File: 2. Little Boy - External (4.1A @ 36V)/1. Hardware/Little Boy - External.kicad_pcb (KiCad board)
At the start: 4 copper layers, 67.2 x 46.8 mm, 65 parts, among them IC1 DRV8251DDAR, IC2 AS5600-ASOT, J10 Conn_01x06_MountingPin, J11 Conn_01x06_MountingPin, J3 Power_In, J4 Power_In, J5 MOT_B, J6 MOT_A, J7 Conn_01x06_MountingPin, J8 Control_In, J9 Control_In, U1 STM32G0B1CBTx, U2 LMR33630CDDA, U3 TLV76733DRVx, U4 TJA1051T-3, U5 MA730, Y1 Crystal_GND24

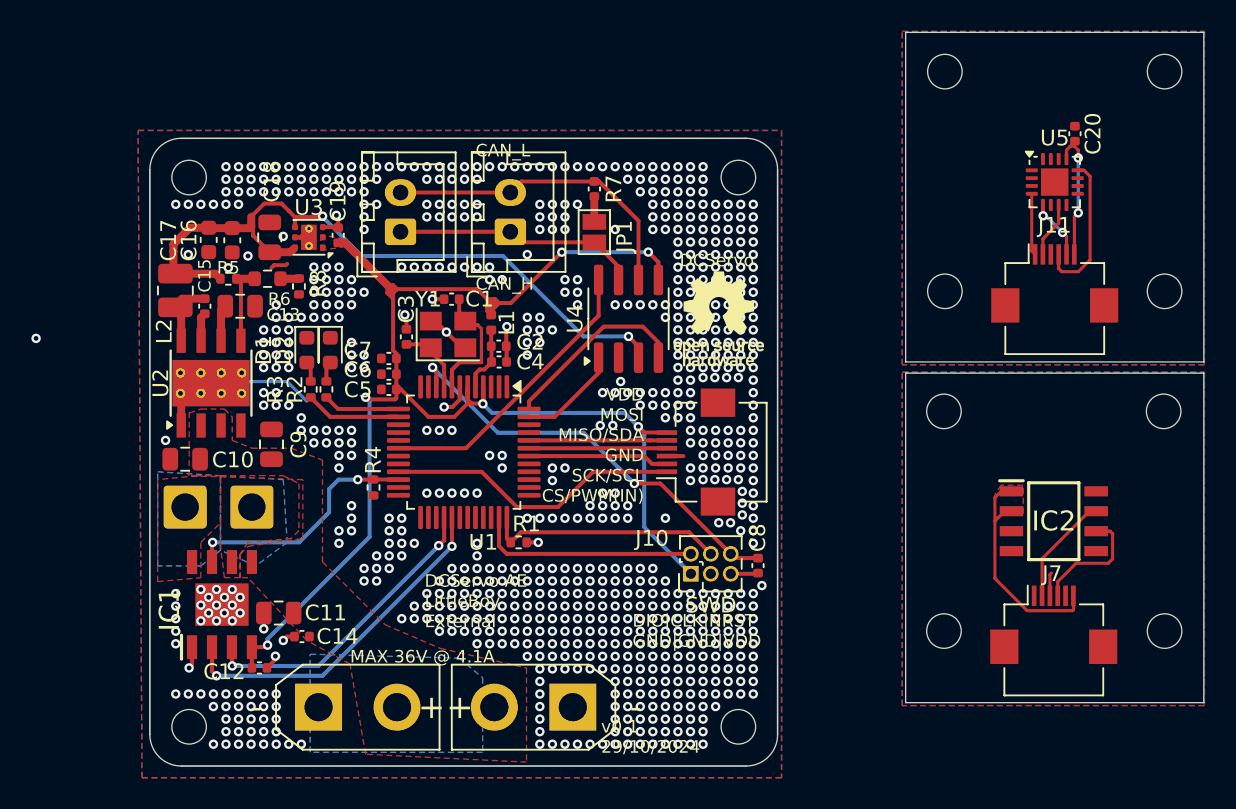
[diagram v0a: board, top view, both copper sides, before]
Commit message: Esthetic Changes, Fix-up of daughter boards.
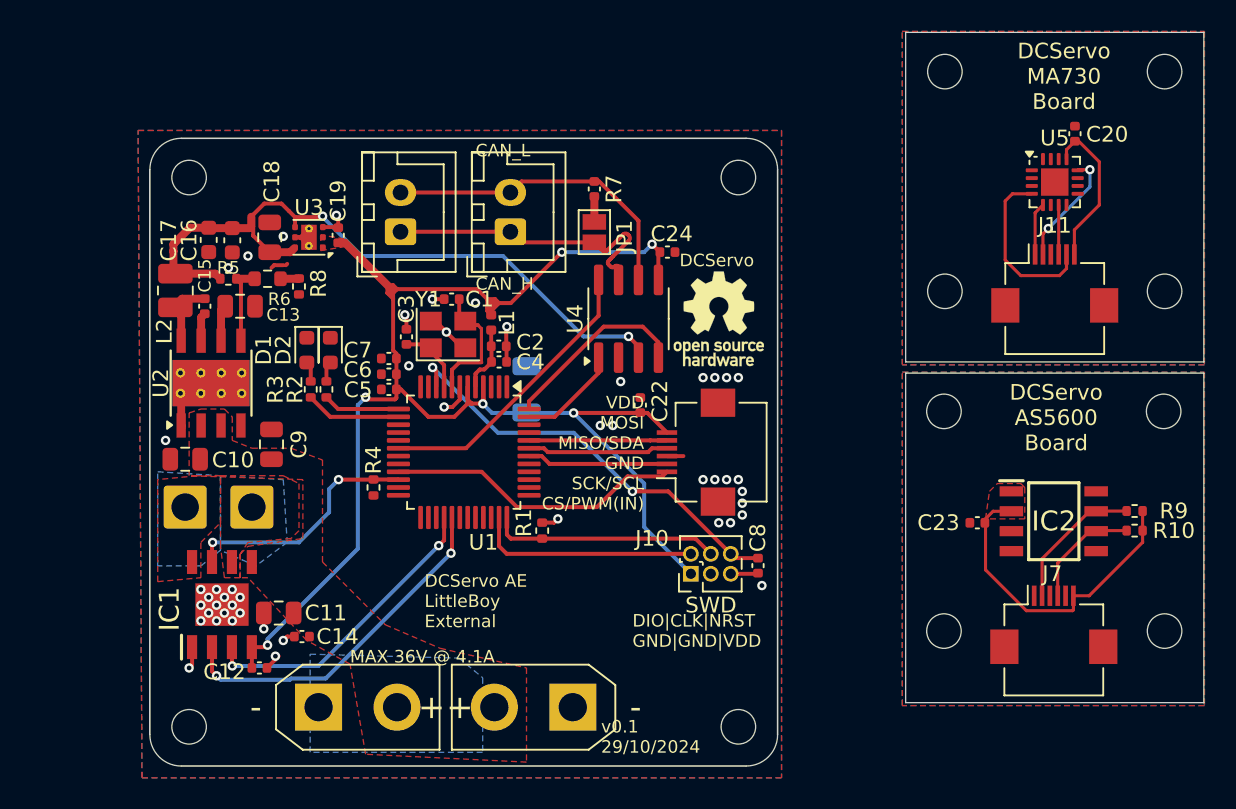
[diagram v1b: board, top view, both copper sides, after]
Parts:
- added C21: 100nF, Capacitor_SMD:C_1206_3216Metric, B.Cu at (147.0, 59.0)
- added C22: 100nF, Capacitor_SMD:C_0402_1005Metric, F.Cu at (154.2, 60.0)
- added C23: 100nF, Capacitor_SMD:C_0402_1005Metric, F.Cu at (175.7, 67.5)
- added C24: 100nF, Capacitor_SMD:C_0402_1005Metric, F.Cu at (156.0, 50.2)
- added R10: 4.7k, Resistor_SMD:R_0402_1005Metric, F.Cu at (185.8, 68.0)
- added R9: 4.7k, Resistor_SMD:R_0402_1005Metric, F.Cu at (185.8, 66.8)
- added REF**: , Symbol:OSHW-Logo_19x20mm_SilkScreen, B.Cu at (180.8, 68.5)
- added REF**: OSHW-Logo_19x20mm_SilkScreen, Symbol:OSHW-Logo_19x20mm_SilkScreen, B.Cu at (180.8, 46.8)
- moved R1 1.68 mm to (148.0, 68.0), turned to 90 degrees
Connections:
- U5 pad 12: Net-(J11-Pin_4) -> Net-(J11-Pin_2)
- U5 pad 4: Net-(J11-Pin_1) -> Net-(J11-Pin_5)
- U5 pad 5: Net-(J11-Pin_5) -> Net-(J11-Pin_1)
- U5 pad 7: Net-(J11-Pin_2) -> Net-(J11-Pin_4)
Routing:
- net Net-(J11-Pin_5): track 4.29 -> 11.0 mm, vias 2 -> 0
- net GND: track 31.3 -> 24.9 mm, vias 770 -> 49
- net Net-(J11-Pin_4): track 9.57 -> 3.15 mm
- net +3.3VP: track 14.4 -> 20.5 mm
- net CAN_H: track 15.7 -> 19.6 mm
- net Net-(J11-Pin_2): track 3.56 -> 7.43 mm, vias 0 -> 2
- net +3V3: track 95.1 -> 98.3 mm
- net Encoder_SCL: track 7.06 -> 9.01 mm
- net +3.3V: track 8.29 -> 10.0 mm, vias 2 -> 0
- net GND2: track 1.49 -> 0.00 mm
- net (no net): track 0.94 -> 0.00 mm, vias 1 -> 0
- net SWCLK: track 15.3 -> 14.6 mm
- net Net-(J11-Pin_1): track 3.95 -> 3.36 mm
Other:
- board text added: "DCServo AS5600 Board"
- board text added: "DCServo MA730 Board"

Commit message: V2.2 - Added Test Points, fixed DFM Errors
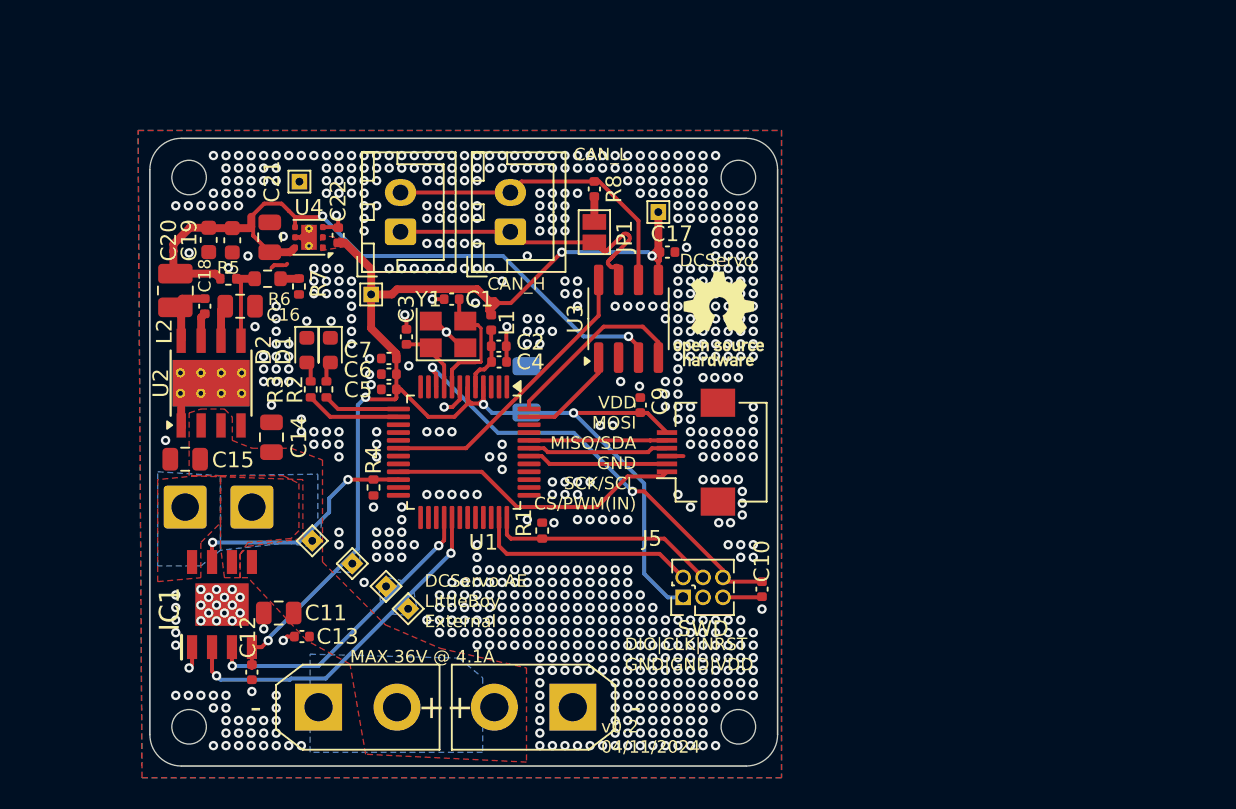
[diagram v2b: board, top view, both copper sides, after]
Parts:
- removed the C20 at (181.9, 42.7)
- removed C23: 100nF, Capacitor_SMD:C_0402_1005Metric
- removed H11, H5, H8, H9: MountingHole, MountingHole:MountingHole_2.2mm_M2
- removed the H12 at (187.7, 74.4)
- removed the H2 at (187.7, 52.8)
- removed the H3 at (173.6, 60.4)
- removed the H6 at (187.6, 60.4)
- removed IC2: AS5600-ASOT, KiCadLibrary:SOIC127P600X175-8N
- removed the J11 at (180.7, 52.2)
- removed R10, R9: 4.7k, Resistor_SMD:R_0402_1005Metric
- removed the REF** at (180.8, 68.5)
- removed the REF** at (180.8, 46.8)
- removed U5: MA730, Package_DFN_QFN:QFN-16-1EP_3x3mm_P0.5mm_EP1.75x1.75mm
- added J1: Conn_01x01, TestPoint:TestPoint_THTPad_1.0x1.0mm_Drill0.5mm, F.Cu at (137.1, 53.0)
- added J12: Conn_01x01, TestPoint:TestPoint_THTPad_1.0x1.0mm_Drill0.5mm, F.Cu at (132.5, 45.8)
- added J17: Conn_01x01, TestPoint:TestPoint_THTPad_1.0x1.0mm_Drill0.5mm, F.Cu at (133.3, 68.7)
- added J2: Conn_01x01, TestPoint:TestPoint_THTPad_1.0x1.0mm_Drill0.5mm, F.Cu at (155.4, 47.7)
- added J3: Conn_01x01, TestPoint:TestPoint_THTPad_1.0x1.0mm_Drill0.5mm, F.Cu at (135.9, 70.1)
- added J6: Conn_01x01, TestPoint:TestPoint_THTPad_1.0x1.0mm_Drill0.5mm, F.Cu at (139.5, 73.0)
- J7: value Conn_01x06_MountingPin -> Conn_01x01; footprint Connector_FFC-FPC:Hirose_FH12-6S-0.5SH_1x06-1MP_P0.50mm_Horizontal -> TestPoint:TestPoint_THTPad_1.0x1.0mm_Drill0.5mm
- moved J7 42.6 mm to (138.1, 71.5), turned to 45 degrees
- moved SWD 1.58 mm to (157.0, 72.2)
- moved C10 1.52 mm to (162.0, 71.7)
- moved C12 0.55 mm to (129.5, 77.0), turned to 90 degrees
- moved C14 0.45 mm to (130.8, 62.0)
- renumbered C8 to C10, C14 to C13, C9 to C14, C10 to C15, C13 to C16, C24 to C17, C15 to C18, C16 to C19, C17 to C20, C18 to C21, C19 to C22, C21 to C8, C22 to C9, D2 to D1, D1 to D2, H4 to H12, H1 to H2, H7 to H3, H10 to H6, J5 to J10, J6 to J11, J8 to J13, J9 to J14, J10 to J5, J3 to J8, J4 to J9, R8 to R7, R7 to R8, U4 to U3, U3 to U4
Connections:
- J7 pad 1: unconnected-(J7-Pin_1-Pad1) -> DRV_IN1
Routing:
- net +3.3VP: track 20.5 -> 0.00 mm
- net Net-(J11-Pin_5): track 11.0 -> 0.00 mm
- net +3.3V: track 10.0 -> 0.00 mm
- net Encoder_SCL: track 9.01 -> 0.00 mm
- net Net-(J11-Pin_2): track 7.43 -> 0.00 mm, vias 2 -> 0
- net Encoder_SDA: track 7.33 -> 0.00 mm
- net +3V3: track 98.3 -> 102.0 mm
- net Net-(J11-Pin_1): track 3.36 -> 0.00 mm
- net Net-(J11-Pin_4): track 3.15 -> 0.00 mm
- net GND: track 24.9 -> 22.5 mm, vias 49 -> 716
- net NRST: track 27.1 -> 28.0 mm
- added copper zone on B.Cu, net +3V3
- added copper zone on B.Cu, net DRV_IN1
- added copper zone on B.Cu, net DRV_IN2
- added copper zone on B.Cu, net ISEN
- removed copper zone on F.Cu, net +3.3VP
- removed copper zone on B.Cu, net GND1
- removed copper zone on F.Cu, net GND1
- removed copper zone on In1.Cu, net GND1
- removed copper zone on In2.Cu, net GND1
- removed copper zone on B.Cu, net GND2
- removed copper zone on F.Cu, net GND2
- removed copper zone on In1.Cu, net GND2
- removed copper zone on In2.Cu, net GND2
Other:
- board size 67.2 x 46.8 mm -> 40 x 40 mm
- board text added: "v0.2 04/11/2024"
- board text removed: "DCServo AS5600 Board"
- board text removed: "DCServo MA730 Board"
- board text removed: "v0.1 29/10/2024"

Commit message: up
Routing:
- net Net-(IC1-OUT2): vias 0 -> 2
- net GND: vias 716 -> 728
- net  MOT_A: vias 0 -> 3
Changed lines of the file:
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@@
 	)
 	(via
+		(at 124 74)
+		(size 0.6)
+		(drill 0.3)
+		(layers "F.Cu" "B.Cu")
+		(free yes)
+		(net 2)
+	)
+	(via
 		(at 147.85 56.1)
 		(size 0.6)
@@
 	)
 	(via
+		(at 125 78)
+		(size 0.6)
+		(drill 0.3)
+		(layers "F.Cu" "B.Cu")
+		(free yes)
+		(net 2)
+	)
+	(via
 		(at 159.05 63.3)
 		(size 0.6)
@@
 	)
 	(via
+		(at 130.5 76)
+		(size 0.6)
+		(drill 0.3)
+		(layers "F.Cu" "B.Cu")
+		(free yes)
+		(net 2)
+	)
+	(via
 		(at 134.887498 47.909178)
 		(size 0.6)
@@
 	)
 	(via
+		(at 124.5 76.5)
+		(size 0.6)
+		(drill 0.3)
+		(layers "F.Cu" "B.Cu")
+		(free yes)
+		(net 2)
+	)
+	(via
 		(at 147.85 73.7)
 		(size 0.6)
@@
 	)
 	(via
+		(at 132.5 76)
+		(size 0.6)
+		(drill 0.3)
+		(layers "F.Cu" "B.Cu")
+		(free yes)
+		(net 2)
+	)
+	(via
 		(at 150.25 52.9)
 		(size 0.6)
@@
 	)
 	(via
+		(at 124 75)
+		(size 0.6)
+		(drill 0.3)
+		(layers "F.Cu" "B.Cu")
+		(free yes)
+		(net 2)
+	)
+	(via
 		(at 153 58.5)
 		(size 0.6)
@@
 	)
 	(via
+		(at 125.5 77.5)
+		(size 0.6)
+		(drill 0.3)
+		(layers "F.Cu" "B.Cu")
+		(free yes)
+		(net 2)
+	)
+	(via
 		(at 148.65 72.1)
 		(size 0.6)
@@
 	)
 	(via
+		(at 131.5 76)
+		(size 0.6)
+		(drill 0.3)
+		(layers "F.Cu" "B.Cu")
+		(free yes)
+		(net 2)
+	)
+	(via
 		(at 157.45 77.7)
 		(size 0.6)
@@
 	)
 	(via
+		(at 124 77)
+		(size 0.6)
+		(drill 0.3)
+		(layers "F.Cu" "B.Cu")
+		(free yes)
+		(net 2)
+	)
+	(via
 		(at 139.05 69.7)
 		(size 0.6)
@@
 	)
 	(via
+		(at 124 72.5)
+		(size 0.6)
+		(drill 0.3)
+		(layers "F.Cu" "B.Cu")
+		(free yes)
+		(net 2)
+	)
+	(via
 		(at 159.05 76.9)
 		(size 0.6)
@@
 	)
 	(via
+		(at 124 76)
+		(size 0.6)
+		(drill 0.3)
+		(layers "F.Cu" "B.Cu")
+		(free yes)
+		(net 2)
+	)
+	(via
 		(at 147.85 81.7)
 		(size 0.6)
@@
 	)
 	(via
+		(at 124.5 77.5)
+		(size 0.6)
+		(drill 0.3)
+		(layers "F.Cu" "B.Cu")
+		(free yes)
+		(net 2)
+	)
+	(via
 		(at 148.65 46.5)
 		(size 0.6)
@@
 		(net 13)
 	)
+	(via
+		(at 124 69)
+		(size 0.6)
+		(drill 0.3)
+		(layers "F.Cu" "B.Cu")
+		(free yes)
+		(net 14)
+	)
+	(via
+		(at 124 70)
+		(size 0.6)
+		(drill 0.3)
+		(layers "F.Cu" "B.Cu")
+		(free yes)
+		(net 14)
+	)
 	(segment
 		(start 142.1875 69.4375)
@@
 		(net 59)
 	)
+	(via
+		(at 132 67.5)
+		(size 0.6)
+		(drill 0.3)
+		(layers "F.Cu" "B.Cu")
+		(free yes)
+		(net 62)
+	)
+	(via
+		(at 132 66.5)
+		(size 0.6)
+		(drill 0.3)
+		(layers "F.Cu" "B.Cu")
+		(free yes)
+		(net 62)
+	)
+	(via
+		(at 132 65.5)
+		(size 0.6)
+		(drill 0.3)
+		(layers "F.Cu" "B.Cu")
+		(free yes)
+		(net 62)
+	)
 	(zone

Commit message: 3
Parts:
- moved J17 2.78 mm to (134.9, 66.3)
- moved J12 1.88 mm to (130.8, 46.6)
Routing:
- net GND: track 22.5 -> 22.6 mm, vias 728 -> 725
